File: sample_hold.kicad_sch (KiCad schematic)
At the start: 44 parts, among them K21 G6K-2FY, 5V, Q201 AO3400A, Q202 AO3401A, Q203 AO3400A, Q204 AO3400A, Q205 AO3400A, Q206 AO3400A, Q207 AO3400A, U19 TCA0372, U21 OPA828DGN, U22 OPA2197D, U23 DG419D

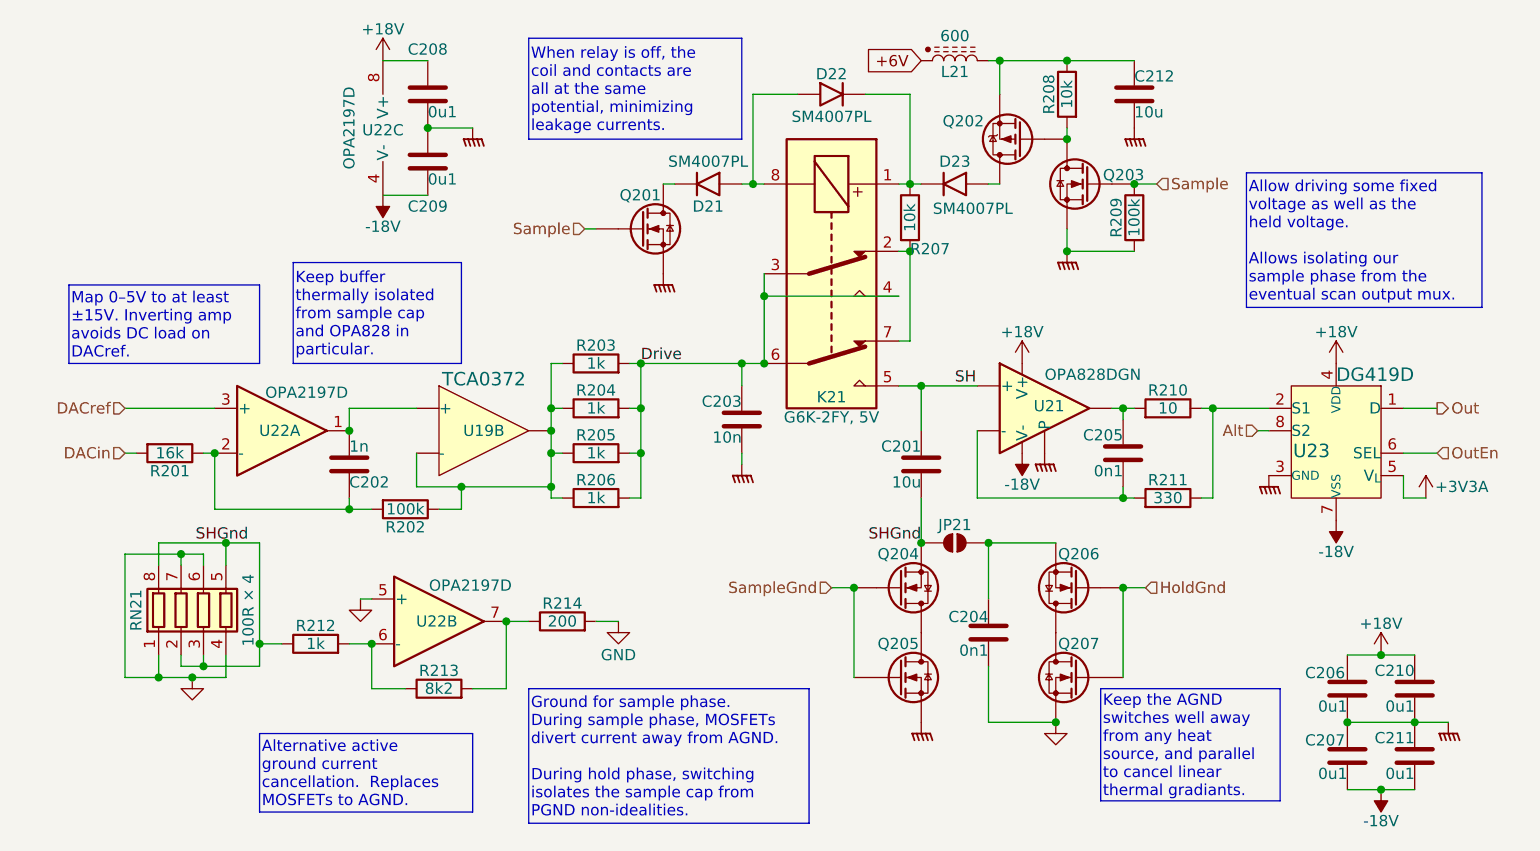
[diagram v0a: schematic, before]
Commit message: Tweaks following spice simulation.
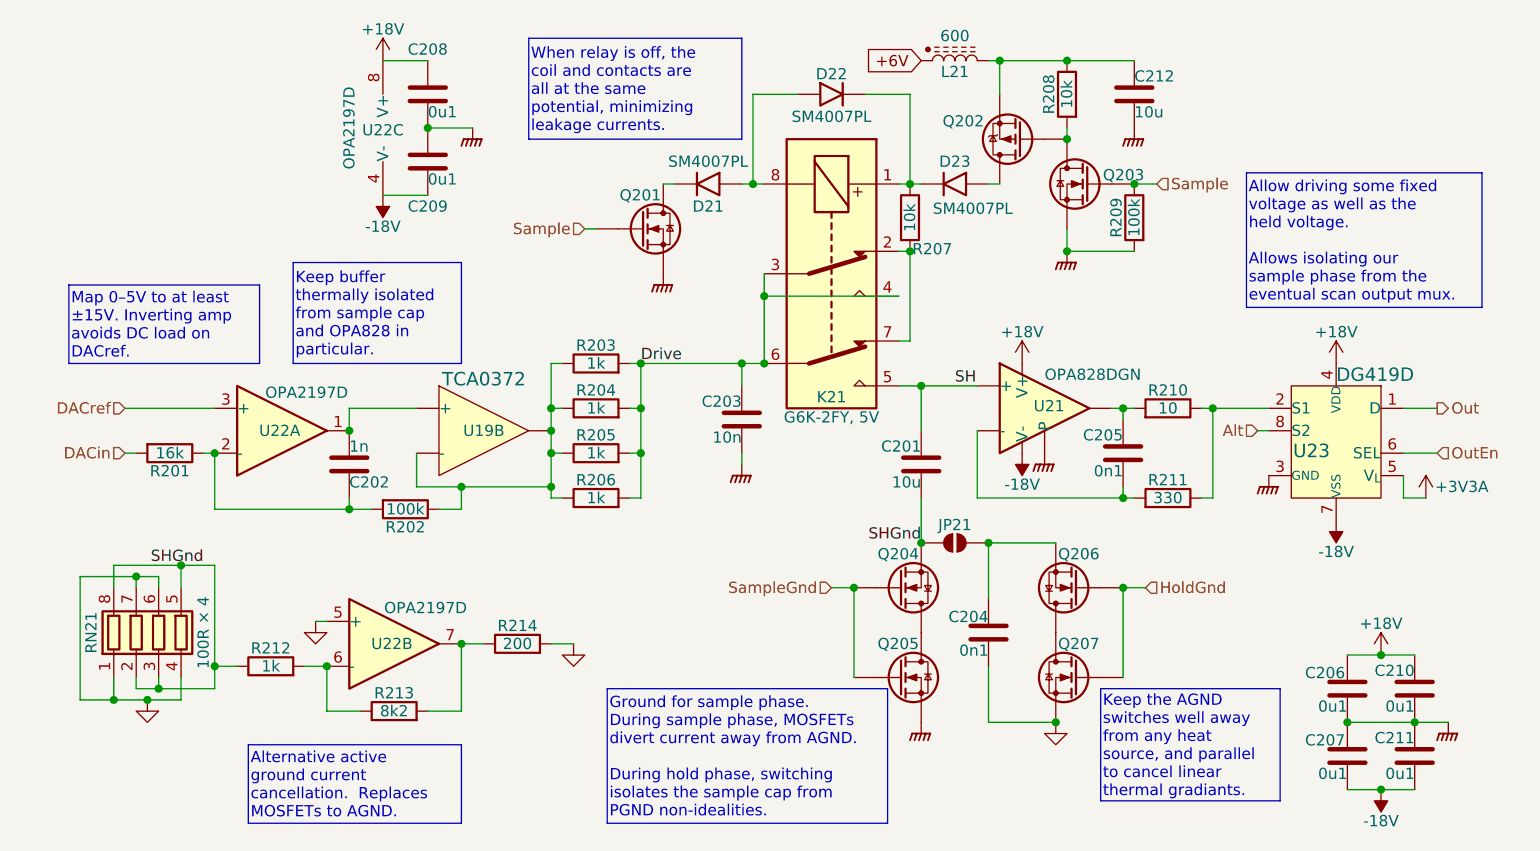
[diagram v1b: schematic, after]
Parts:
- JP21: footprint Parts:ThermJump_1 -> Parts:JumperOpen
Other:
- moved on the sheet: R212, R213, R214, RN21, U22B

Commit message: About to delete scan...
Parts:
- C201: Stock (none) -> 5
- C202: value 1n -> 0n1; LCSC C1523 -> C1546
- C212: value 10u -> 1u; footprint Capacitor_SMD:C_0603_1608Metric -> Capacitor_SMD:C_0402_1005Metric; LCSC C96446 -> C52923
- RN21: Stock (none) -> 100
- U19: Stock (none) -> 3
- U22: Stock (none) -> 30

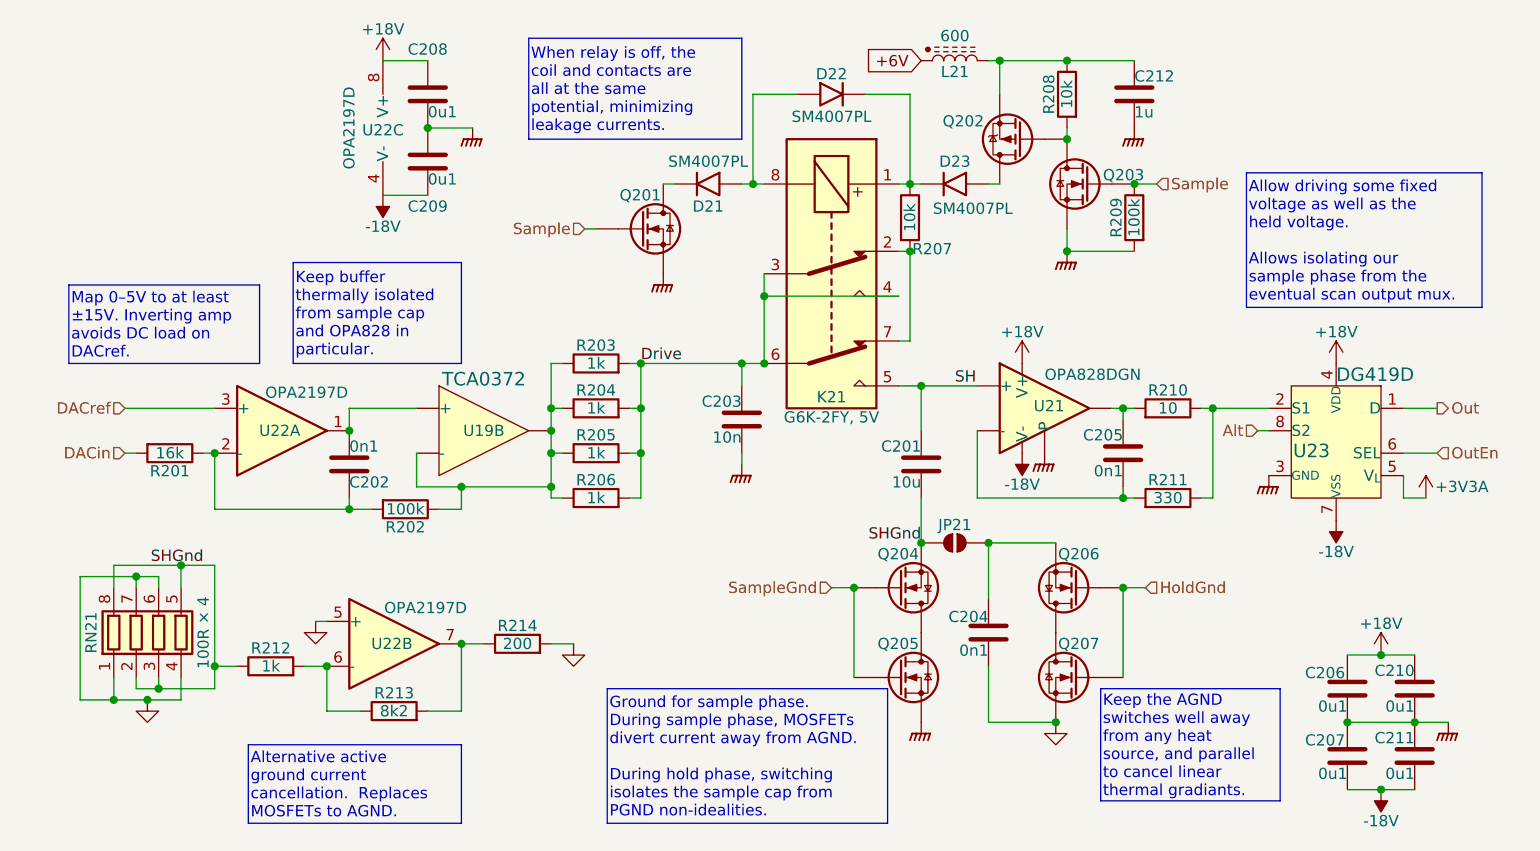
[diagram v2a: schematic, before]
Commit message: S&H restored.  Now to touch up connections etc.
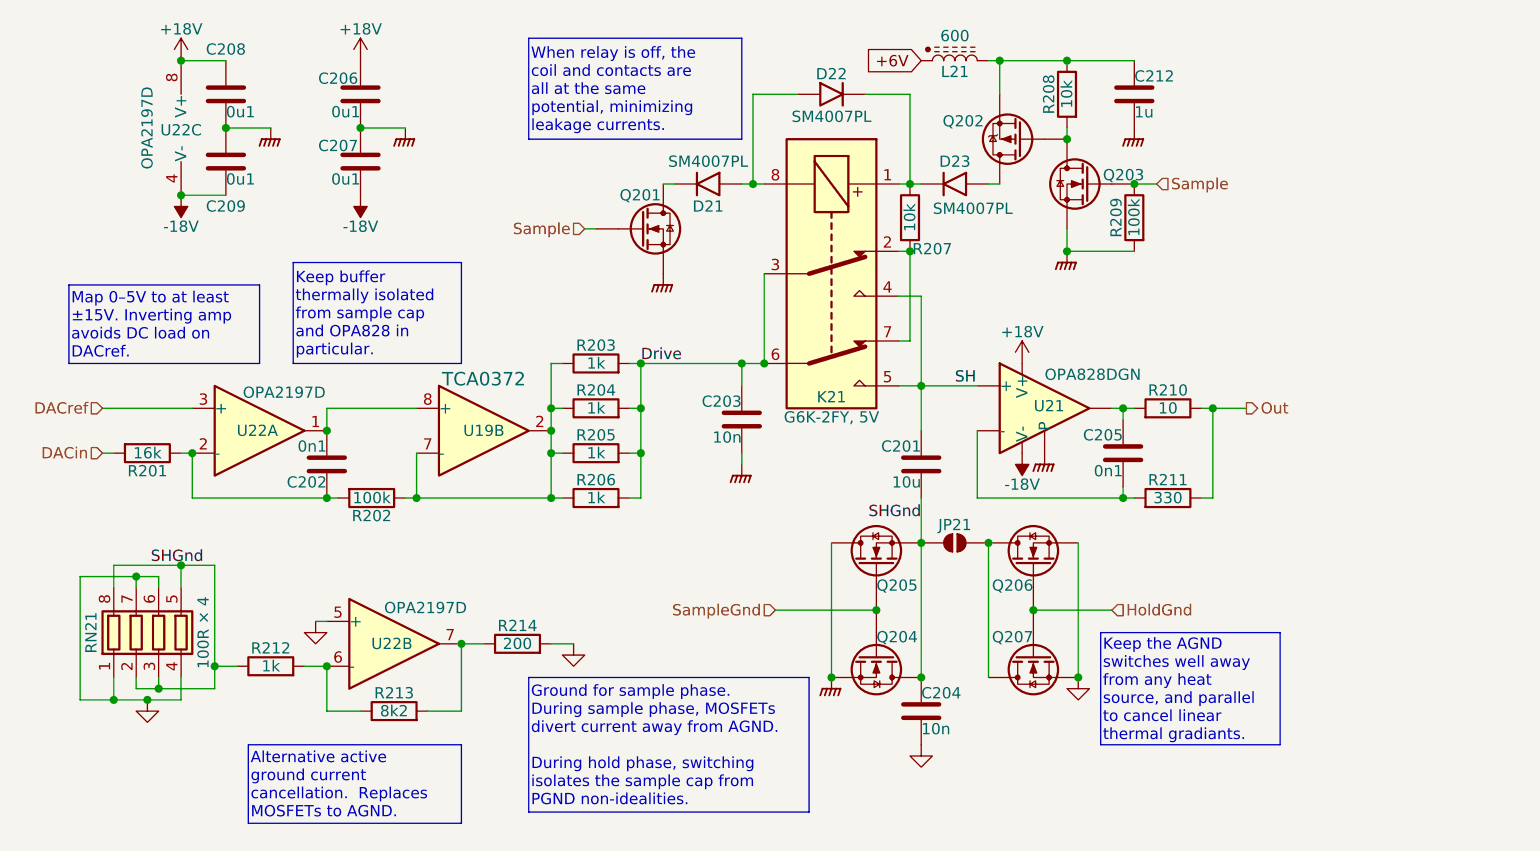
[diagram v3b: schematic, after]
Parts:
- removed C210, C211: 0u1, Capacitor_SMD:C_0402_1005Metric, symbol Device:C
- removed U23: DG419D, Package_SO:SOIC-8_3.9x4.9mm_P1.27mm, symbol Parts:DG419
- C204: value 0n1 -> 10n; footprint Capacitor_SMD:C_0402_1005Metric -> (none); LCSC C1546 -> (none)
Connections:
- net Drive: no longer K21.4
- net GND: now also Q206.2 (S)
- net GNDPWR: now also Q204.2 (S), Q205.3 (D); no longer Q205.2 (S)
- net Out: now also R210.1, R211.1
- net SH: now also K21.4
- net SHGnd: now also C204.1, Q204.3 (D), Q205.2 (S); no longer Q204.2 (S)
- net at Q206.3 (D), Q207.3 (D): now also JP21.2 (B)
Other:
- moved on the sheet: C202, C204, C206, C207, C208, C209, Q204, Q205, Q206, Q207, R201, R202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

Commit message: Put ref filtering into the schematic.
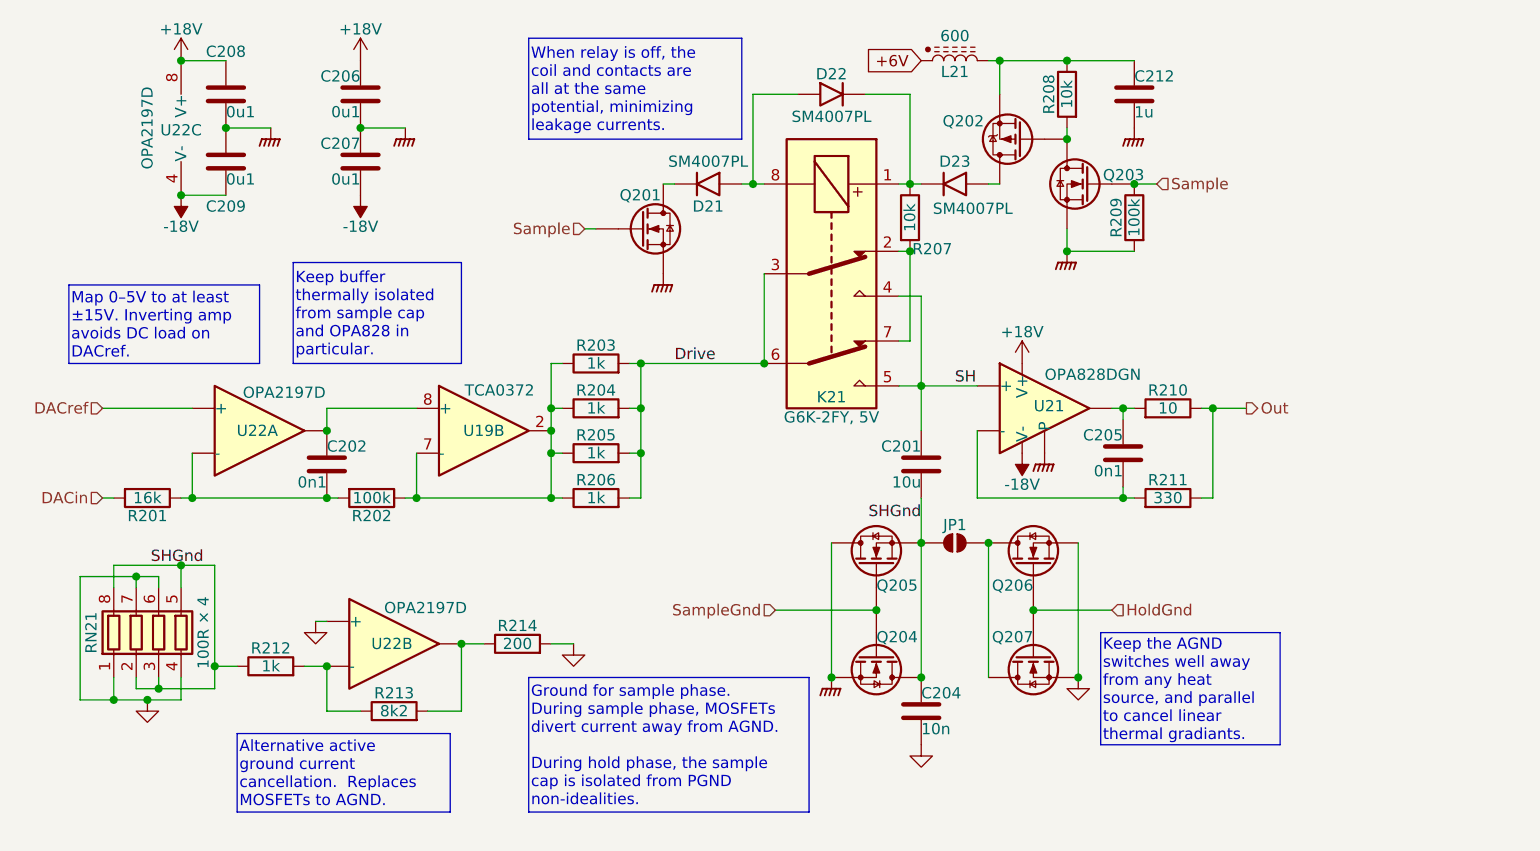
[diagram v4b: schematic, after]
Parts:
- removed C203: 10n, Capacitor_SMD:C_0603_1608Metric, symbol Device:C
- renumbered JP21 to JP1
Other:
- moved on the sheet: R201

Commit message: Adjust voltage rails.
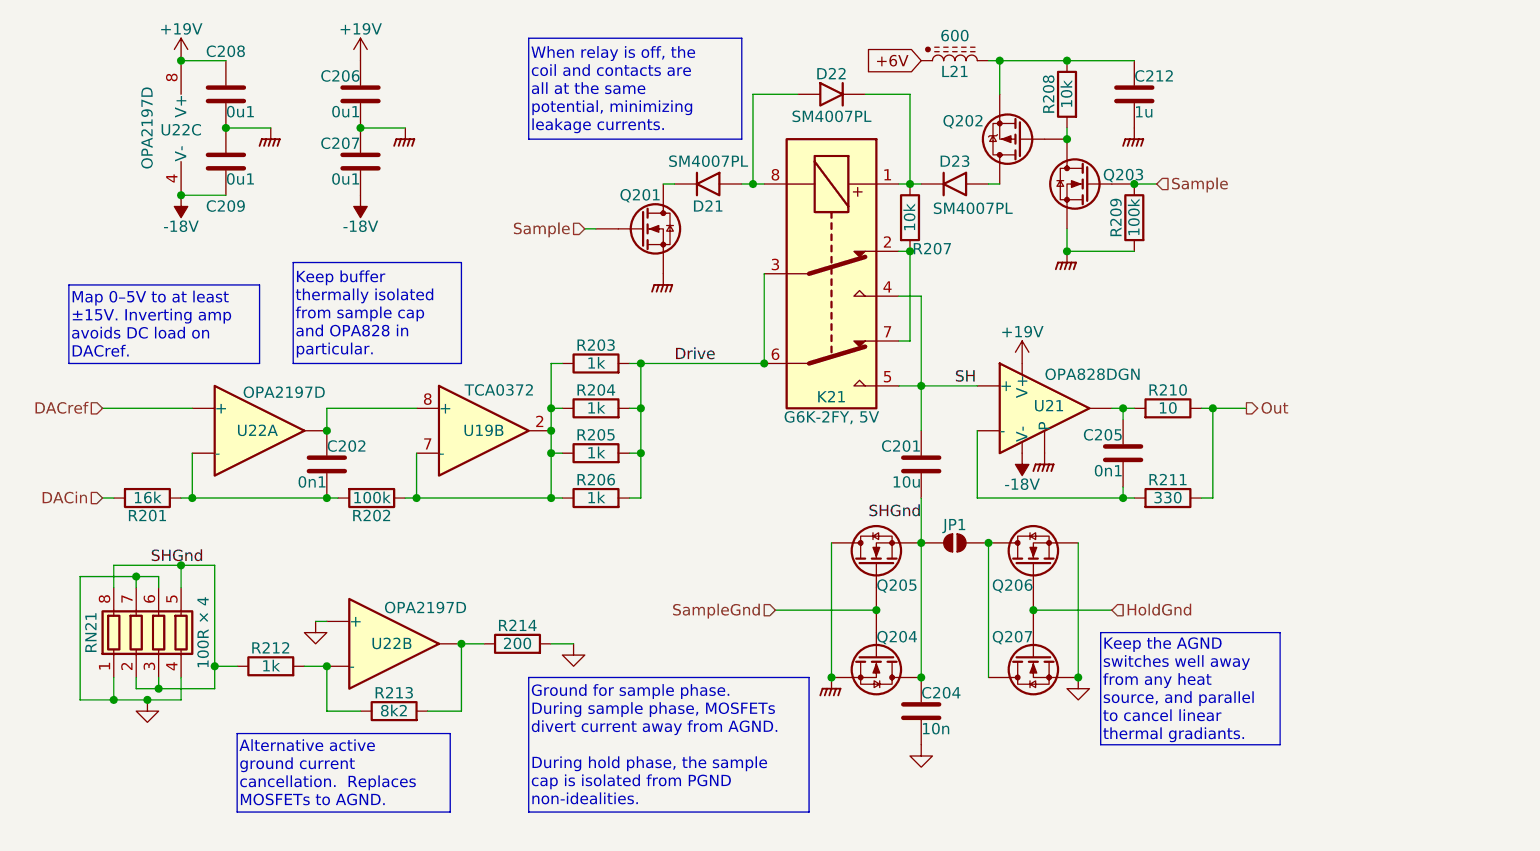
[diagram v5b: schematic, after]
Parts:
- C204: footprint (none) -> Capacitor_SMD:C_0603_1608Metric; LCSC (none) -> C307500
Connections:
- net +18V renamed +19V
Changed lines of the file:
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@@
 	)
 	(symbol
-		(lib_id "Parts:+18V")
+		(lib_id "Parts:+19V")
 		(at 177.8 62.23 0)
 		(unit 1)
@@
 		(on_board yes)
 		(dnp no)
-		(property "Reference" "#PWR098"
+		(property "Reference" "#PWR98"
 			(at 177.8 66.04 0)
 			(effects
@@
 			)
 		)
-		(property "Value" "+18V"
+		(property "Value" "+19V"
 			(at 177.8 58.674 0)
 			(do_not_autoplace yes)
@@
 			)
 		)
-		(property "Description" "Power symbol creates a global label with name {dblquote}+18V{dblquote}"
+		(property "Description" "Power symbol creates a global label with name \"+19\""
 			(at 177.8 62.23 0)
 			(effects
@@
 			(project "lincal"
 				(path "/b054cef4-39e3-49d8-aff0-7ba5a206c187/6f91b1d1-06a0-428d-b546-bc9bd4fa19a0"
-					(reference "#PWR0100")
+					(reference "#PWR100")
 					(unit 1)
 				)
 				(path "/b054cef4-39e3-49d8-aff0-7ba5a206c187/8eaf15be-2df7-401b-a518-33a048754894"
-					(reference "#PWR098")
+					(reference "#PWR98")
 					(unit 1)
 				)
@@
 	)
 	(symbol
-		(lib_id "Parts:+18V")
+		(lib_id "Parts:+19V")
 		(at 102.87 27.94 0)
 		(unit 1)
@@
 		(on_board yes)
 		(dnp no)
-		(property "Reference" "#PWR0328"
+		(property "Reference" "#PWR328"
 			(at 102.87 31.75 0)
 			(effects
@@
 			)
 		)
-		(property "Value" "+18V"
+		(property "Value" "+19V"
 			(at 102.87 24.384 0)
 			(do_not_autoplace yes)
@@
 			)
 		)
-		(property "Description" "Power symbol creates a global label with name {dblquote}+18V{dblquote}"
+		(property "Description" "Power symbol creates a global label with name \"+19\""
 			(at 102.87 27.94 0)
 			(effects
@@
 			(project "lincal"
 				(path "/b054cef4-39e3-49d8-aff0-7ba5a206c187/6f91b1d1-06a0-428d-b546-bc9bd4fa19a0"
-					(reference "#PWR0330")
+					(reference "#PWR330")
 					(unit 1)
 				)
 				(path "/b054cef4-39e3-49d8-aff0-7ba5a206c187/8eaf15be-2df7-401b-a518-33a048754894"
-					(reference "#PWR0328")
+					(reference "#PWR328")
 					(unit 1)
 				)
@@
 			)
 		)
-		(property "Footprint" ""
+		(property "Footprint" "Capacitor_SMD:C_0603_1608Metric"
 			(at 167.3352 105.41 0)
 			(effects
@@
 			)
 		)
-		(property "Datasheet" ""
+		(property "Datasheet" "C0G, 25V"
 			(at 166.37 101.6 0)
 			(effects
@@
 			)
 		)
-		(property "LCSC" ""
+		(property "LCSC" "C307500"
 			(at 166.37 101.6 0)
 			(effects
@@
 	)
 	(symbol
-		(lib_id "Parts:+18V")
+		(lib_id "Parts:+19V")
 		(at 82.55 27.94 0)
 		(unit 1)
@@
 		(on_board yes)
 		(dnp no)
-		(property "Reference" "#PWR081"
+		(property "Reference" "#PWR81"
 			(at 82.55 31.75 0)
 			(effects
@@
 			)
 		)
-		(property "Value" "+18V"
+		(property "Value" "+19V"
 			(at 82.55 24.384 0)
 			(do_not_autoplace yes)
@@
 			)
 		)
-		(property "Description" "Power symbol creates a global label with name {dblquote}+18V{dblquote}"
+		(property "Description" "Power symbol creates a global label with name \"+19\""
 			(at 82.55 27.94 0)
 			(effects
@@
 			(project "lincal"
 				(path "/b054cef4-39e3-49d8-aff0-7ba5a206c187/6f91b1d1-06a0-428d-b546-bc9bd4fa19a0"
-					(reference "#PWR091")
+					(reference "#PWR91")
 					(unit 1)
 				)
 				(path "/b054cef4-39e3-49d8-aff0-7ba5a206c187/8eaf15be-2df7-401b-a518-33a048754894"
-					(reference "#PWR081")
+					(reference "#PWR81")
 					(unit 1)
 				)
